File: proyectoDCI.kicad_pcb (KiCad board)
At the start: 2 copper layers, 45 x 20 mm, 27 parts, among them P1 CONN_02X04, P2 CONN_01X01, P3 GSG-RF-CONN, P4 GSG-RF-CONN, U1 AD5933, U2 ADG849, U3 AD8606, U4 ASFLMB-16.000MHZ-LY-T, U5 ADP150

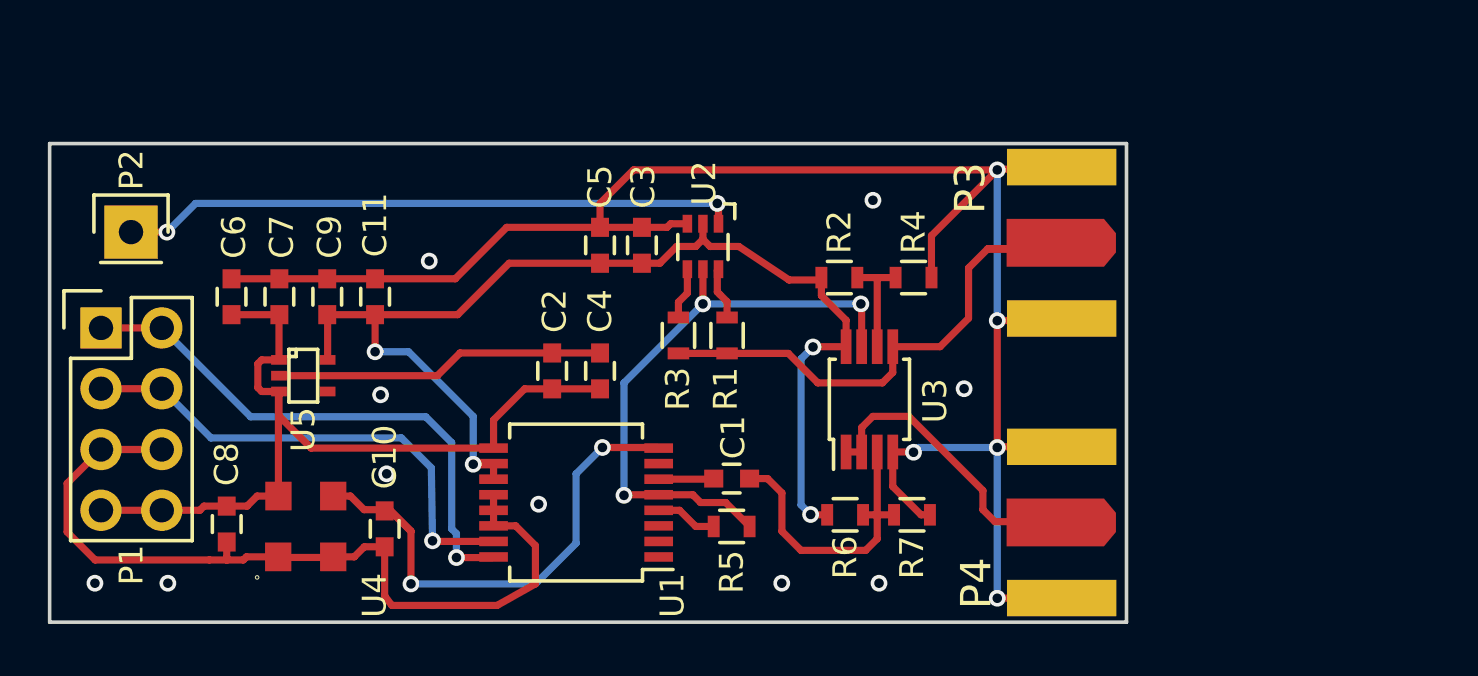
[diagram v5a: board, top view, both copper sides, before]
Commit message: Correcciones sugeridas por la 2da revision efectuada por D. Brengi
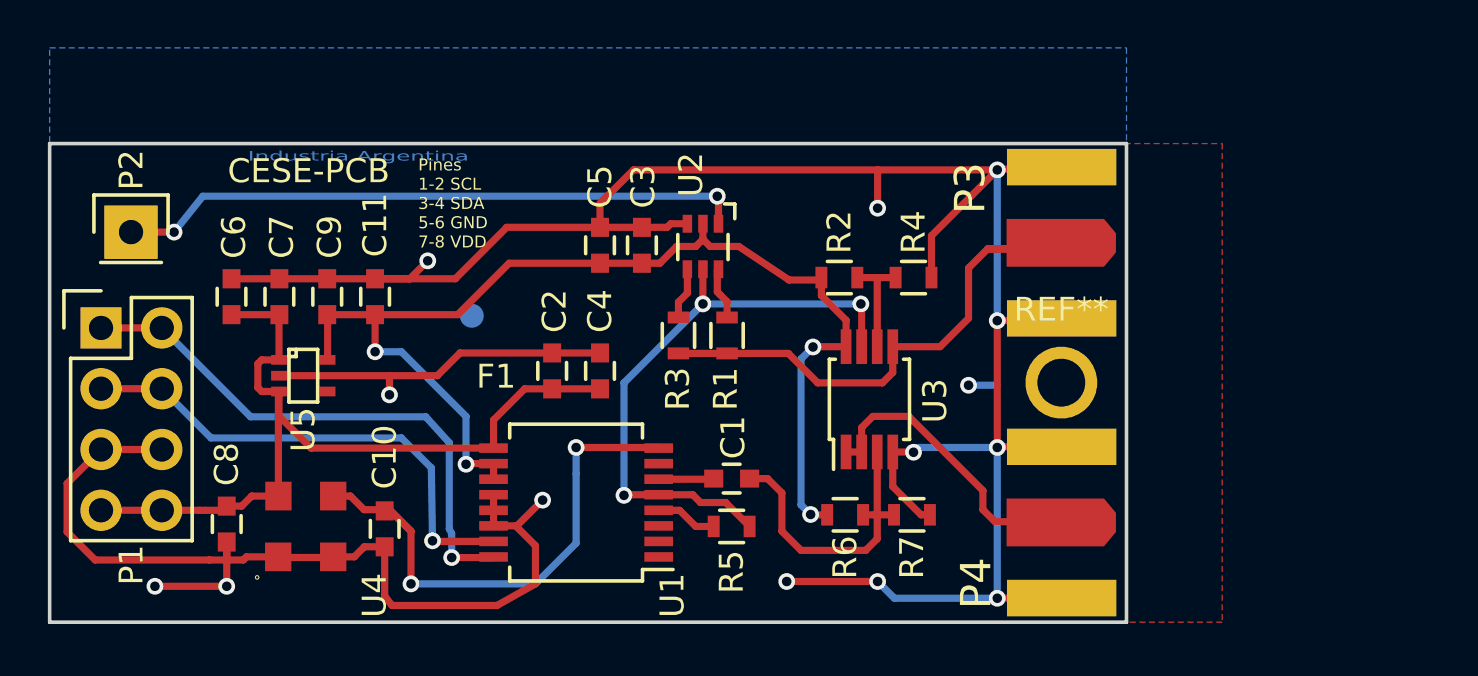
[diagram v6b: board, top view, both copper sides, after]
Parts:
- added F1: Fiducial_1mm_Dia_2.54mm_Outer_CopperTop, Fiducials:Fiducial_1mm_Dia_2.54mm_Outer_CopperTop, F.Cu at (167.6, 107.7)
- added REF**: 1pin, Connectors:1pin, F.Cu at (192.3, 110.5)
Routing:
- net GND: track 129.5 -> 149.9 mm, vias 5 -> 13
- net (no net): track 0.00 -> 1.20 mm, vias 10 -> 1
- net /Otros/MCLK: track 22.1 -> 22.8 mm
- net /Senal/SEL: track 25.9 -> 26.4 mm
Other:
- board text added: "CESE-PCB"
- board text added: "Grilla de posicionamiento : 0,2 mm Grilla de ruteo : 0,1 mm"
- board text added: "Industria Argentina"
- board text added: "Pines 1-2 SCL 3-4 SDA 5-6 GND 7-8 VDD"
- board text removed: "Medidor de impedancia v1.0"
